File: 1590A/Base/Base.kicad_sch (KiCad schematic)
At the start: 22 parts, among them J101 Barrel_Jack_Switch, J102 AudioJack2_Ground, J103 AudioJack2_Ground, J104 Conn_01x04_Pin, J105 Conn_01x04_Pin, J106 Conn_01x04_Pin, Q101 DMC3071LVT, Q102 BC846

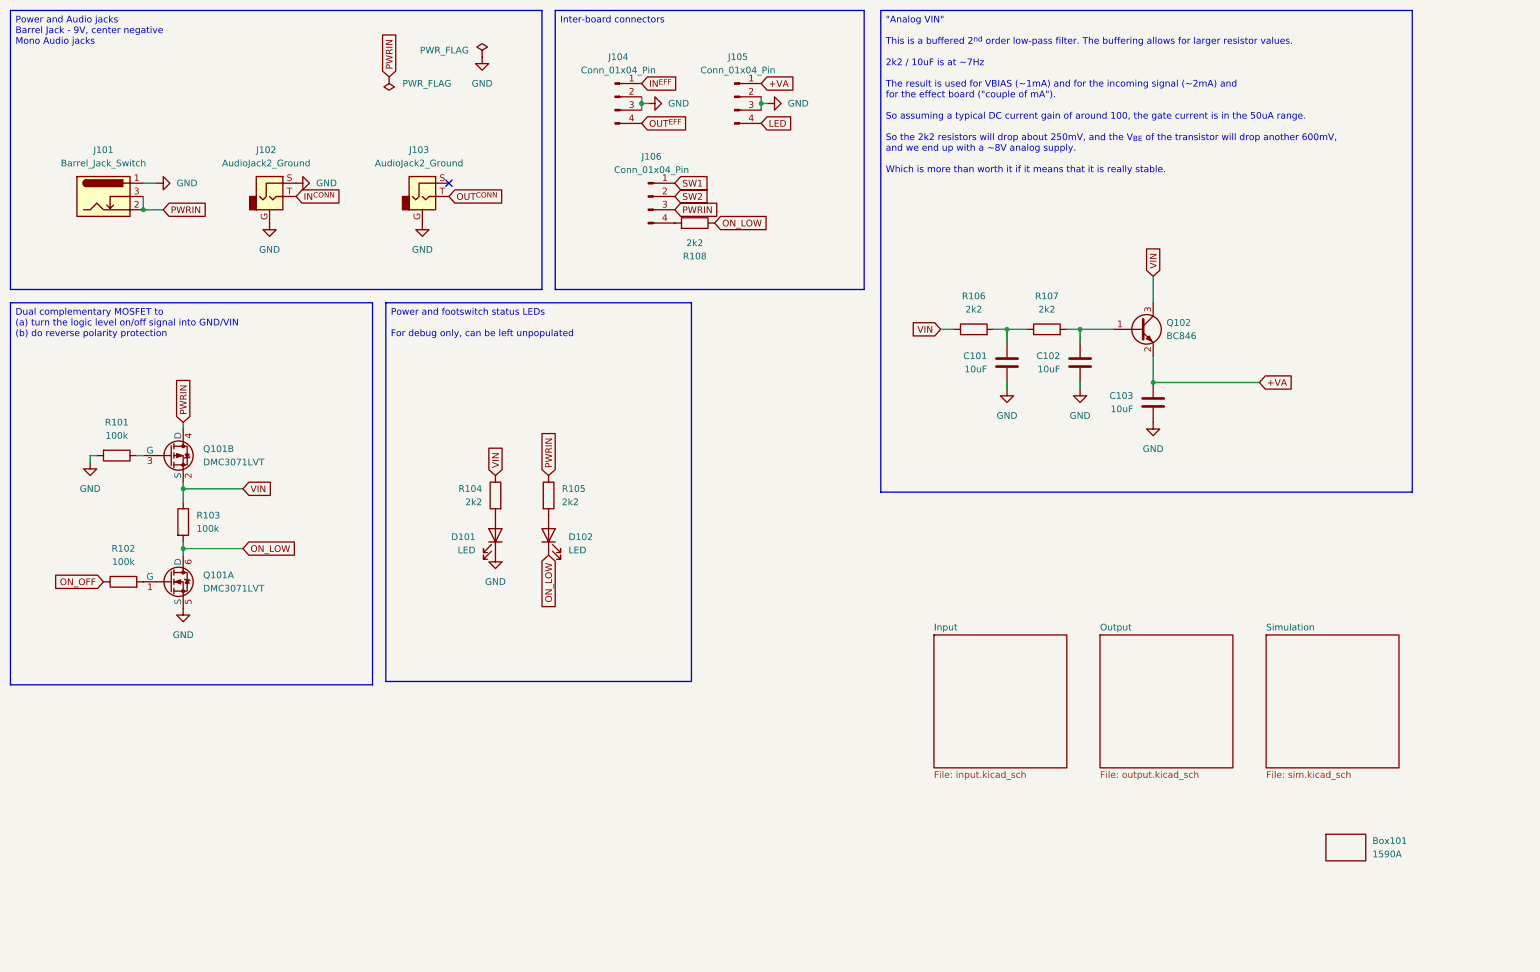
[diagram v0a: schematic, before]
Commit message: Update 1590A board
I really wanted to use the stomp switch board, but I didn't find any
sane connectors that are convenient and fit.

So I just updated this board to have the stomp switch directly on the
board instead.  I'd love to re-use stomp switches after I have made a
(bad) design and tested it, but the pain just doesn't seem worth it.

That means that I could just have used a traditional latching 3PDT, but
instead this sticks to the electronic switching with a momentary switch.
Because the whole point is the circuit, not sanity.

Add another openscad 3d model for this stomp switch thing.

Signed-off-by: Linus Torvalds <torvalds@linux-foundation.org>
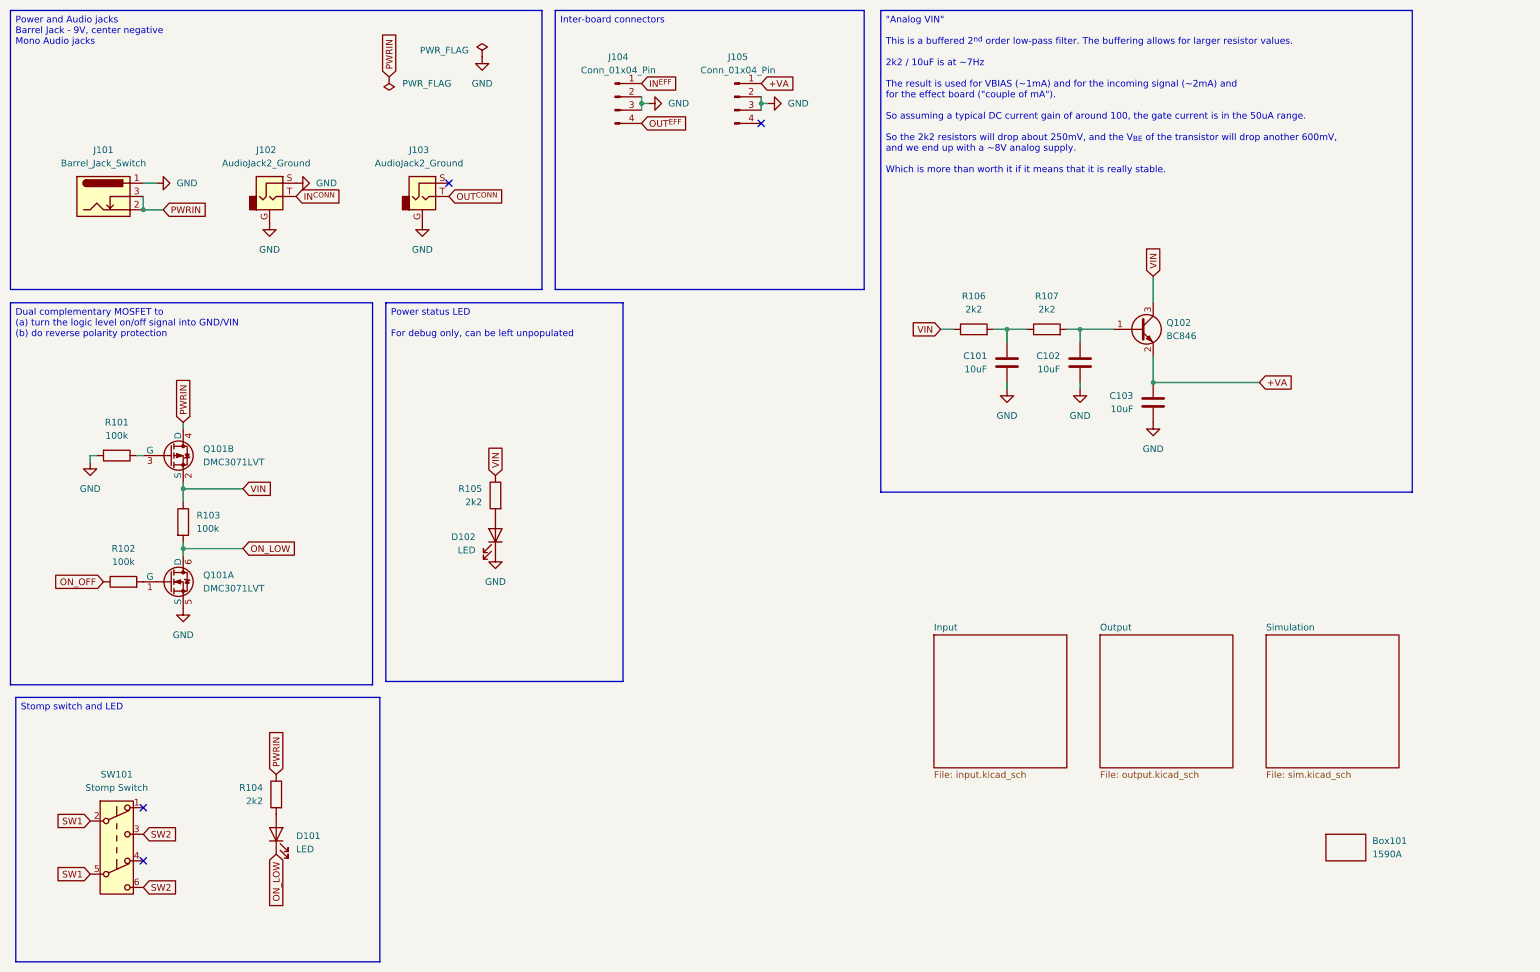
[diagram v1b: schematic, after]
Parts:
- removed D102: LED, LED_SMD:LED_0805_2012Metric, symbol Device:LED
- removed J106: Conn_01x04_Pin, Connector_PinHeader_1.27mm:PinHeader_1x04_P1.27mm_Horizontal, symbol Connector:Conn_01x04_Pin
- removed R105, R108: 2k2, Resistor_SMD:R_0805_2012Metric, symbol Device:R
- added D101: LED, LED_THT:LED_D5.0mm, symbol Device:LED
- added R104: 2k2, Resistor_SMD:R_0805_2012Metric, symbol Device:R
- added SW101: Stomp Switch, Mylib:FS5700DPMT2B2M2QE, symbol Switch:SW_Push_DPDT
- J101: footprint Connector_BarrelJack:BarrelJack_CLIFF_FC681465S_SMT_Horizontal -> Mylib:Wurth WR-DC 2.1mm Power Jack
- renumbered D101 to D102, R104 to R105
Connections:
- net ON_LOW: now also D101.1 (K)
- net PWRIN: now also R104.1
- net SW1: now also SW101.2 (B), SW101.5 (B)
- net SW2: now also SW101.3 (C), SW101.6 (C)
- net LED: no longer names the net of J105.4 (Pin_4)
- new net: D101.2 (A), R104.2
- no-connect marks 1 -> 4

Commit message: Another try at cleaning up project path handling
The removed TOPLEVEL hackery also tried to deal with the problem of
finding the spice models for simulation, which had the same confusion
with project-specific files and no sane kicad model that I could find
for it.

This attempts to deal with it by just making a 'spice' symlink from the
"kicad project" directory to the "real project" directory, and dealing
with the spice model paths that way.

Signed-off-by: Linus Torvalds <torvalds@linux-foundation.org>
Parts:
- removed Q102: BC846, Package_TO_SOT_SMD:SOT-23, symbol Transistor_BJT:BC846
- added Q1: BC846, Package_TO_SOT_SMD:SOT-23, symbol Mylib:BC846
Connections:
- net +VA: now also Q1.2 (E)
- net VIN: now also Q1.3 (C)
- net at C102.1, R107.2: now also Q1.1 (B)
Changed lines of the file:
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@@
 			)
 		)
-		(property "Sim.Library" "${KIPRJMOD}/../../symbols/DMC3071LVT.lib"
+		(property "Sim.Library" "spice/DMC3071LVT.lib"
 			(at 49.53 105.41 0)
 			(effects
@@
 			)
 		)
-		(property "Sim.Library" "${KIPRJMOD}/../../symbols/DMC3071LVT.lib"
+		(property "Sim.Library" "spice/DMC3071LVT.lib"
 			(at 49.53 129.54 0)
 			(effects
@@
 	)
 	(symbol
-		(lib_id "Transistor_BJT:BC846")
-		(at 229.87 74.93 0)
-		(unit 1)
-		(exclude_from_sim no)
-		(in_bom yes)
-		(on_board yes)
-		(dnp no)
-		(fields_autoplaced yes)
-		(property "Reference" "Q102"
-			(at 234.95 73.6599 0)
-			(effects
-				(font
-					(size 1.27 1.27)
-				)
-				(justify left)
-			)
-		)
-		(property "Value" "BC846"
-			(at 234.95 76.1999 0)
-			(effects
-				(font
-					(size 1.27 1.27)
-				)
-				(justify left)
-			)
-		)
-		(property "Footprint" "Package_TO_SOT_SMD:SOT-23"
-			(at 234.95 76.835 0)
-			(effects
-				(font
-					(size 1.27 1.27)
-					(italic yes)
-				)
-				(justify left)
-				(hide yes)
-			)
-		)
-		(property "Datasheet" "https://assets.nexperia.com/documents/data-sheet/BC846_SER.pdf"
-			(at 229.87 74.93 0)
-			(effects
-				(font
-					(size 1.27 1.27)
-				)
-				(justify left)
-				(hide yes)
-			)
-		)
-		(property "Description" "0.1A Ic, 65V Vce, NPN Transistor, SOT-23"
-			(at 229.87 74.93 0)
-			(effects
-				(font
-					(size 1.27 1.27)
-				)
-				(hide yes)
-			)
-		)
-		(property "Sim.Library" "/home/torvalds/KiCad/sim/BC846.txt"
-			(at 229.87 74.93 0)
-			(effects
-				(font
-					(size 1.27 1.27)
-				)
-				(hide yes)
-			)
-		)
-		(property "Sim.Name" "BC846"
-			(at 229.87 74.93 0)
-			(effects
-				(font
-					(size 1.27 1.27)
-				)
-				(hide yes)
-			)
-		)
-		(property "Sim.Device" "SUBCKT"
-			(at 229.87 74.93 0)
-			(effects
-				(font
-					(size 1.27 1.27)
-				)
-				(hide yes)
-			)
-		)
-		(property "Sim.Pins" "1=2 2=3 3=1"
-			(at 229.87 74.93 0)
-			(effects
-				(font
-					(size 1.27 1.27)
-				)
-				(hide yes)
-			)
-		)
-		(pin "2"
-		)
-		(pin "3"
-		)
-		(pin "1"
-		)
-		(instances
-			(project "Jacks"
-				(path "/9e337e0b-885b-4d2b-99a2-62cdd082c615"
-					(reference "Q102")
-					(unit 1)
-				)
-			)
-		)
-	)
-	(symbol
 		(lib_id "power:GND")
 		(at 232.41 92.71 0)
@@
 					(unit 1)
 				)
+			)
+		)
+	)
+	(symbol
+		(lib_id "Mylib:BC846")
+		(at 229.87 74.93 0)
+		(unit 1)
+		(exclude_from_sim no)
+		(in_bom yes)
+		(on_board yes)
+		(dnp no)
+		(fields_autoplaced yes)
+		(property "Reference" "Q1"
+			(at 234.95 73.6599 0)
+			(effects
+				(font
+					(size 1.27 1.27)
+				)
+				(justify left)
+			)
+		)
+		(property "Value" "BC846"
+			(at 234.95 76.1999 0)
+			(effects
+				(font
+					(size 1.27 1.27)
+				)
+				(justify left)
+			)
+		)
+		(property "Footprint" "Package_TO_SOT_SMD:SOT-23"
+			(at 229.87 62.23 0)
+			(effects
+				(font
+					(size 1.27 1.27)
+				)
+				(hide yes)
+			)
+		)
+		(property "Datasheet" "https://assets.nexperia.com/documents/data-sheet/BC846X-Q_SER.pdf"
+			(at 229.87 87.63 0)
+			(effects
+				(font
+					(size 1.27 1.27)
+				)
+				(hide yes)
+			)
+		)
+		(property "Description" "NPN transistor, base/emitter/collector"
+			(at 229.87 59.69 0)
+			(effects
+				(font
+					(size 1.27 1.27)
+				)
+				(hide yes)
+			)
+		)
+		(property "Sim.Library" "spice/BC846A.lib"
+			(at 229.87 95.25 0)
+			(effects
+				(font
+					(size 1.27 1.27)
+				)
+				(hide yes)
+			)
+		)
+		(property "Sim.Name" "BC846A"
+			(at 231.14 90.17 0)
+			(effects
+				(font
+					(size 1.27 1.27)
+				)
+				(justify left)
+				(hide yes)
+			)
+		)
+		(property "Sim.Device" "SUBCKT"
+			(at 228.6 90.17 0)
+			(effects
+				(font
+					(size 1.27 1.27)
+				)
+				(justify right)
+				(hide yes)
+			)
+		)
+		(property "Sim.Pins" "1=B 2=E 3=C"
+			(at 229.87 92.71 0)
+			(effects
+				(font
+					(size 1.27 1.27)
+				)
+				(hide yes)
+			)
+		)
+		(pin "3"
+		)
+		(pin "1"
+		)
+		(pin "2"
+		)
+		(instances
+			(project ""
+				(path "/9e337e0b-885b-4d2b-99a2-62cdd082c615"
+					(reference "Q1")
+					(unit 1)
+				)

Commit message: 1590A: Replace the compact footswitch with a regular sized one
The bigger one probably fits better, since we have to reach up past the
audio jacks anyway.

I suspect I will go back to the actual 3PDT true bypass model for this
board, though.  The electronic switching is more interesting, but let's
face it, the simpler circuit with a physical switching of the signal is
simply more practical.

Signed-off-by: Linus Torvalds <torvalds@linux-foundation.org>
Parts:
- removed SW101: Stomp Switch, Mylib:FS5700DPMT2B2M2QE, symbol Switch:SW_Push_DPDT
- added SW101: SW_Push_SPDT, Mylib:PBS-24-102P, symbol Switch:SW_Push_SPDT
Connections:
- net SW1: now also SW101.2 (B)
- net SW2: now also SW101.3 (C)
- no-connect marks 4 -> 3
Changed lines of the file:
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@@
 	)
 	(no_connect
-		(at 39.37 176.53)
-	)
-	(no_connect
 		(at 97.79 46.99)
 	)
@@
 		)
 	)
-	(global_label "SW2"
-		(shape input)
-		(at 39.37 181.61 0)
-		(fields_autoplaced yes)
-		(effects
-			(font
-				(size 1.27 1.27)
-			)
-			(justify left)
-		)
-		(property "Intersheetrefs" "${INTERSHEET_REFS}"
-			(at 46.2256 181.61 0)
-			(effects
-				(font
-					(size 1.27 1.27)
-				)
-				(justify left)
-				(hide yes)
-			)
-		)
-	)
 	(global_label "VIN"
 		(shape input)
@@
 		)
 	)
-	(global_label "SW1"
-		(shape input)
-		(at 29.21 179.07 180)
-		(fields_autoplaced yes)
-		(effects
-			(font
-				(size 1.27 1.27)
-			)
-			(justify right)
-		)
-		(property "Intersheetrefs" "${INTERSHEET_REFS}"
-			(at 22.3544 179.07 0)
-			(effects
-				(font
-					(size 1.27 1.27)
-				)
-				(justify right)
-				(hide yes)
-			)
-		)
-	)
 	(global_label "ON_OFF"
 		(shape input)
@@
 	)
 	(symbol
-		(lib_id "Switch:SW_Push_DPDT")
-		(at 34.29 173.99 0)
-		(unit 1)
-		(exclude_from_sim yes)
-		(in_bom yes)
-		(on_board yes)
-		(dnp no)
-		(fields_autoplaced yes)
-		(property "Reference" "SW101"
-			(at 34.29 160.02 0)
-			(effects
-				(font
-					(size 1.27 1.27)
-				)
-			)
-		)
-		(property "Value" "Stomp Switch"
-			(at 34.29 162.56 0)
-			(effects
-				(font
-					(size 1.27 1.27)
-				)
-			)
-		)
-		(property "Footprint" "Mylib:FS5700DPMT2B2M2QE"
-			(at 34.29 168.91 0)
-			(effects
-				(font
-					(size 1.27 1.27)
-				)
-				(hide yes)
-			)
-		)
-		(property "Datasheet" "~"
-			(at 34.29 168.91 0)
-			(effects
-				(font
-					(size 1.27 1.27)
-				)
-				(hide yes)
-			)
-		)
-		(property "Description" "Momentary Switch, dual pole double throw"
-			(at 34.29 173.99 0)
-			(effects
-				(font
-					(size 1.27 1.27)
-				)
-				(hide yes)
-			)
-		)
-		(pin "3"
-		)
-		(pin "6"
-		)
-		(pin "1"
-		)
-		(pin "5"
-		)
-		(pin "2"
-		)
-		(pin "4"
-		)
-		(instances
-			(project ""
-				(path "/9e337e0b-885b-4d2b-99a2-62cdd082c615"
-					(reference "SW101")
-					(unit 1)
-				)
-			)
-		)
-	)
-	(symbol
 		(lib_id "power:GND")
 		(at 232.41 92.71 0)
@@
 					(unit 1)
 				)
+			)
+		)
+	)
+	(symbol
+		(lib_id "Switch:SW_Push_SPDT")
+		(at 34.29 168.91 0)
+		(unit 1)
+		(exclude_from_sim no)
+		(in_bom yes)
+		(on_board yes)
+		(dnp no)
+		(fields_autoplaced yes)
+		(property "Reference" "SW101"
+			(at 34.29 160.02 0)
+			(effects
+				(font
+					(size 1.27 1.27)
+				)
+			)
+		)
+		(property "Value" "SW_Push_SPDT"
+			(at 34.29 162.56 0)
+			(effects
+				(font
+					(size 1.27 1.27)
+				)
+			)
+		)
+		(property "Footprint" "Mylib:PBS-24-102P"
+			(at 34.29 168.91 0)
+			(effects
+				(font
+					(size 1.27 1.27)
+				)
+				(hide yes)
+			)
+		)
+		(property "Datasheet" "~"
+			(at 34.29 168.91 0)
+			(effects
+				(font
+					(size 1.27 1.27)
+				)
+				(hide yes)
+			)
+		)
+		(property "Description" "Momentary Switch, single pole double throw"
+			(at 34.29 168.91 0)
+			(effects
+				(font
+					(size 1.27 1.27)
+				)
+				(hide yes)
+			)
+		)
+		(pin "3"
+		)
+		(pin "1"
+		)
+		(pin "2"
+		)
+		(instances
+			(project ""
+				(path "/9e337e0b-885b-4d2b-99a2-62cdd082c615"
+					(reference "SW101")
+					(unit 1)
+				)
